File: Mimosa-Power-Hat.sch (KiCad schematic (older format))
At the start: 71 parts, among them J1 Screw_Terminal_01x04, J2 Screw_Terminal_01x02, J3 40HAT, J4 Screw_Terminal_01x02, J5 Screw_Terminal_01x04, J9 CONN_01X02, M1 Fan_Tacho_PWM, Q1 DMG2305UX, Q2 DMMT5401, U1 ADM3490ExR, U2 CAT24C32, U3 TCAN330, U5 AB0805, U6 MCP2515-xSO, U7 TXB0102DCU, U8 LM2678, Y1 32.768 kHz, Y2 8MHz

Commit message: Small update
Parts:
- added C?: 100nF, Capacitor_SMD:C_0805_2012Metric_Pad1.15x1.40mm_HandSolder, symbol Device:C
- added C?: C, Capacitor_SMD:C_0805_2012Metric_Pad1.15x1.40mm_HandSolder, symbol Device:C
- added D? (x4): LED, symbol Device:LED
- added J?: Screw_Terminal_01x02, TerminalBlock_Phoenix:TerminalBlock_Phoenix_MKDS-3-2-5.08_1x02_P5.08mm_Horizontal, symbol Connector:Screw_Terminal_01x02
- added R?: 250R, Resistor_SMD:R_0805_2012Metric_Pad1.15x1.40mm_HandSolder, symbol Device:R_Small
- added R? (x5): 1.2k, Resistor_SMD:R_0805_2012Metric_Pad1.15x1.40mm_HandSolder, symbol Device:R_Small
- added U?: H11L1, symbol Isolator:H11L1
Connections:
- net +3V3: now also C?.2, R?.2, R?.2, U?.6
- net +5V: now also R?.2
- net GND: now also C?.1, D?.1 (K), D?.1 (K), D?.1 (K), D?.1 (K), U?.5
- net P5V: now also R?.2
- net CLK-OUT: now reaches J3.33 (BCM13)
- net CLK-OUT: now also U6.3 (CLKOUT/SOF)
- net SeaTalk1: now reaches J3.37 (BCM26)
- net SeaTalk1: now also R?.1, U?.4
- new net: C?.1, R?.1, U?.1
- new net: D?.2 (A), R?.1 (x4)
- new net ST-Data: C?.2, J?.1 (Pin_1), R?.2, R?.2
- new net ST-GND: J?.2 (Pin_2), U?.2
- no-connect marks 30 -> 27
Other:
- note added: "SeaTalk 1 Read data"

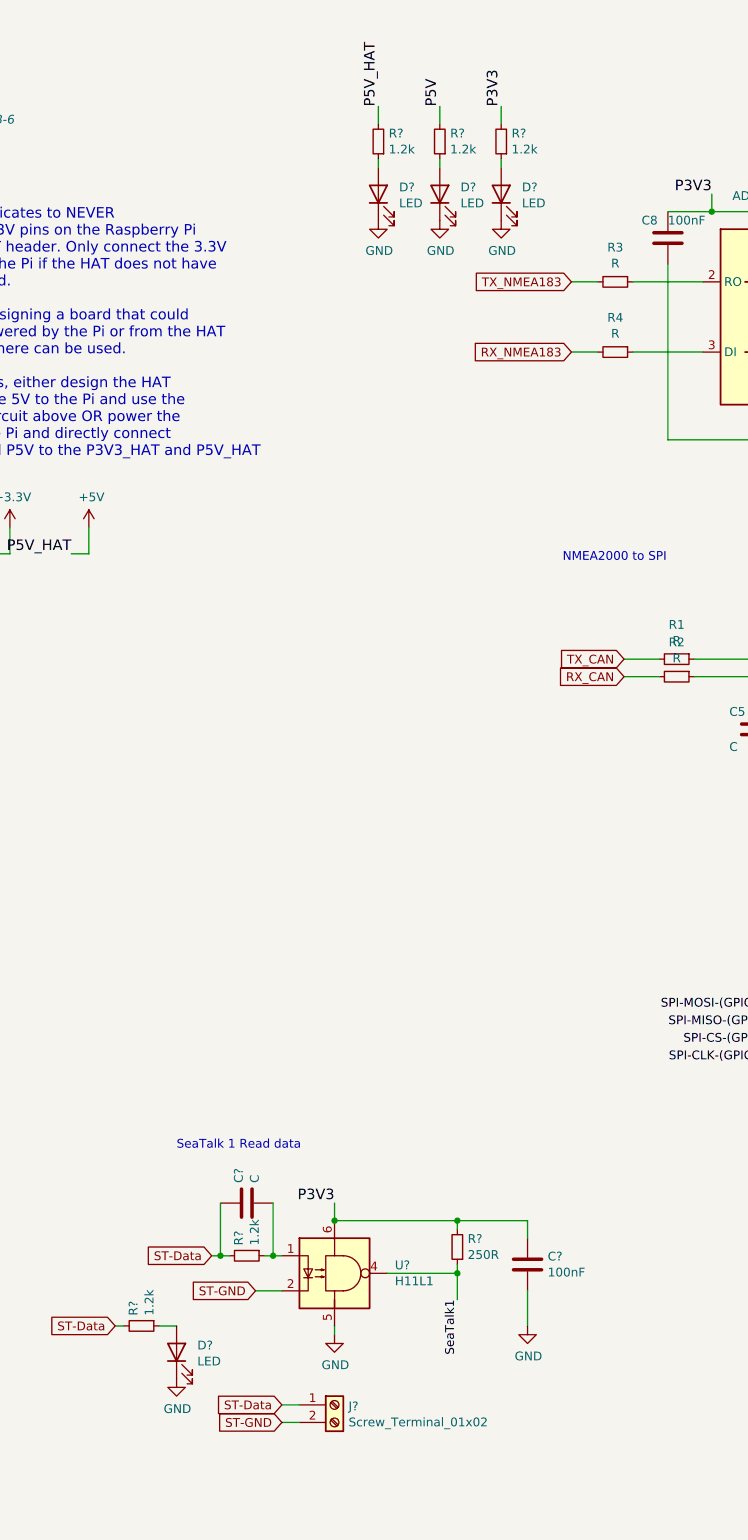
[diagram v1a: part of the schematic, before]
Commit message: Correction of NMEA2000 RX/TX inversion, addition of seatalk circuit connection (not yet routed)
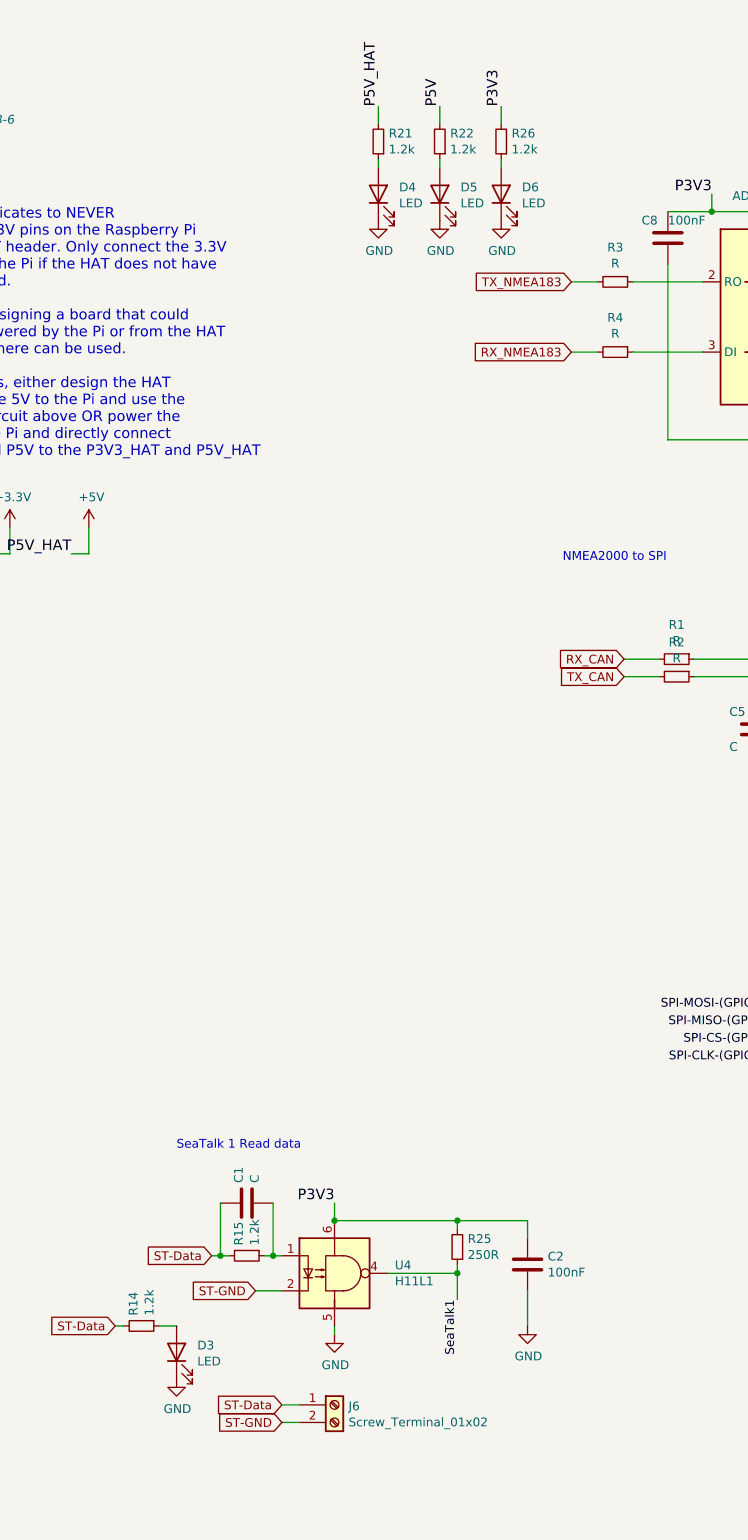
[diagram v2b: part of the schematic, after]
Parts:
- C1, C2: renamed from C?; footprint Capacitor_SMD:C_0805_2012Metric_Pad1.15x1.40mm_HandSolder -> Capacitor_SMD:C_0805_2012Metric_Pad1.18x1.45mm_HandSolder
- C11, C12, C13, C19, C20, C21, C22, C23, C24, C25, C26, C27, C5, C7, C8: footprint Capacitor_SMD:C_0805_2012Metric_Pad1.15x1.40mm_HandSolder -> Capacitor_SMD:C_0805_2012Metric_Pad1.18x1.45mm_HandSolder
- C32, C33: footprint Capacitor_SMD:C_0805_2012Metric -> Capacitor_SMD:C_0805_2012Metric_Pad1.18x1.45mm_HandSolder
- D3, D4, D5, D6: renamed from D?; footprint (none) -> LED_SMD:LED_0805_2012Metric
- R1, R10, R11, R12, R13, R16, R17, R18, R19, R2, R20, R23, R24, R29, R3, R4, R5, R6, R7, R8, R9: footprint Resistor_SMD:R_0805_2012Metric_Pad1.15x1.40mm_HandSolder -> Resistor_SMD:R_0805_2012Metric_Pad1.20x1.40mm_HandSolder
- R14, R15, R21, R22, R25, R26: renamed from R?; footprint Resistor_SMD:R_0805_2012Metric_Pad1.15x1.40mm_HandSolder -> Resistor_SMD:R_0805_2012Metric_Pad1.20x1.40mm_HandSolder
- U4: renamed from U?; footprint (none) -> Package_DIP:DIP-6_W7.62mm_LongPads
- gave numbers to parts that had none: 1
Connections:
- net RX_CAN: now also R1.2; no longer R2.2
- net TX_CAN: now also R2.2; no longer R1.2

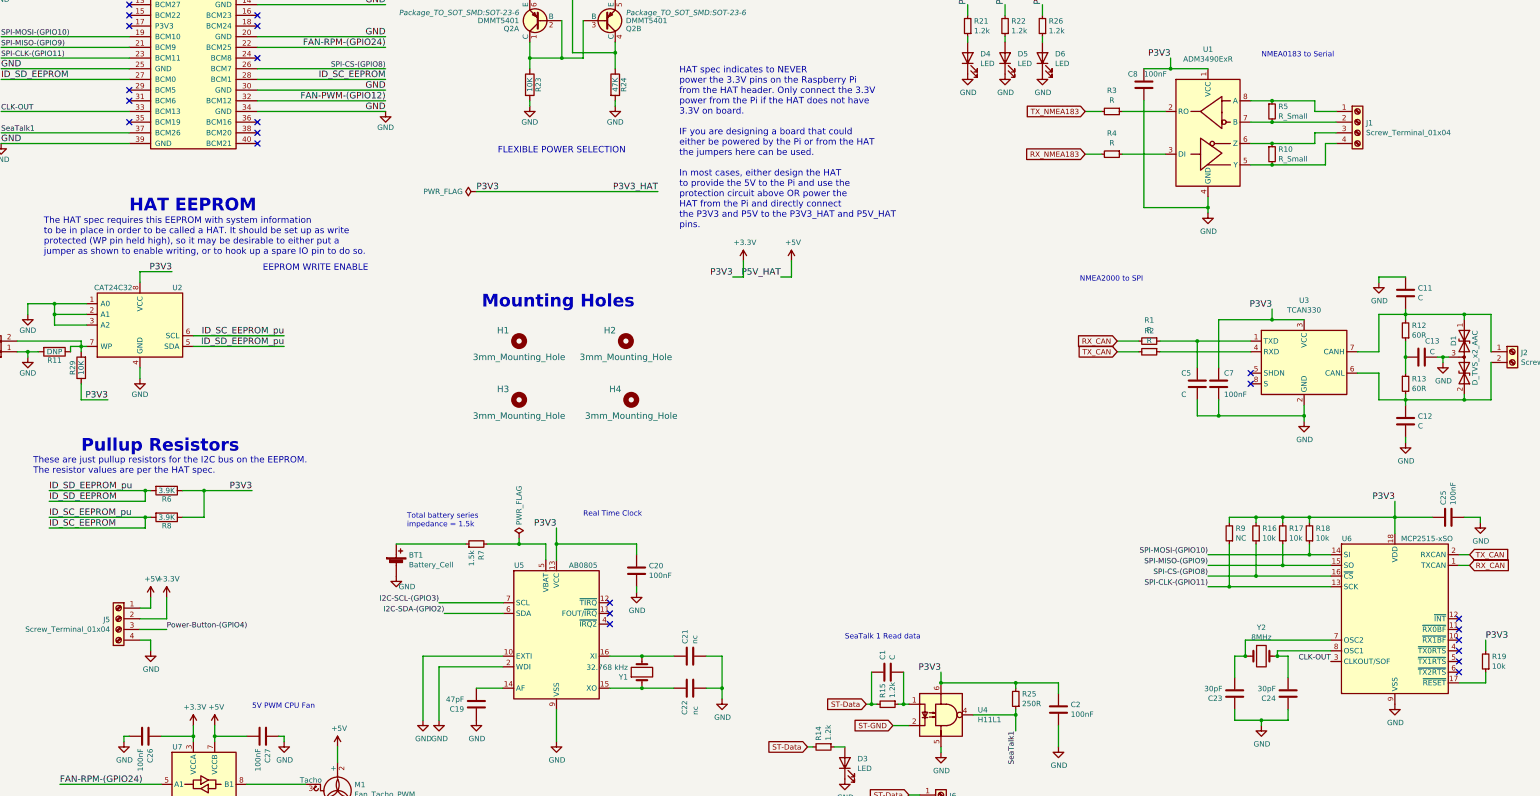
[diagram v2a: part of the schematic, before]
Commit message: add connection for seatalk, cleaned board and schematic
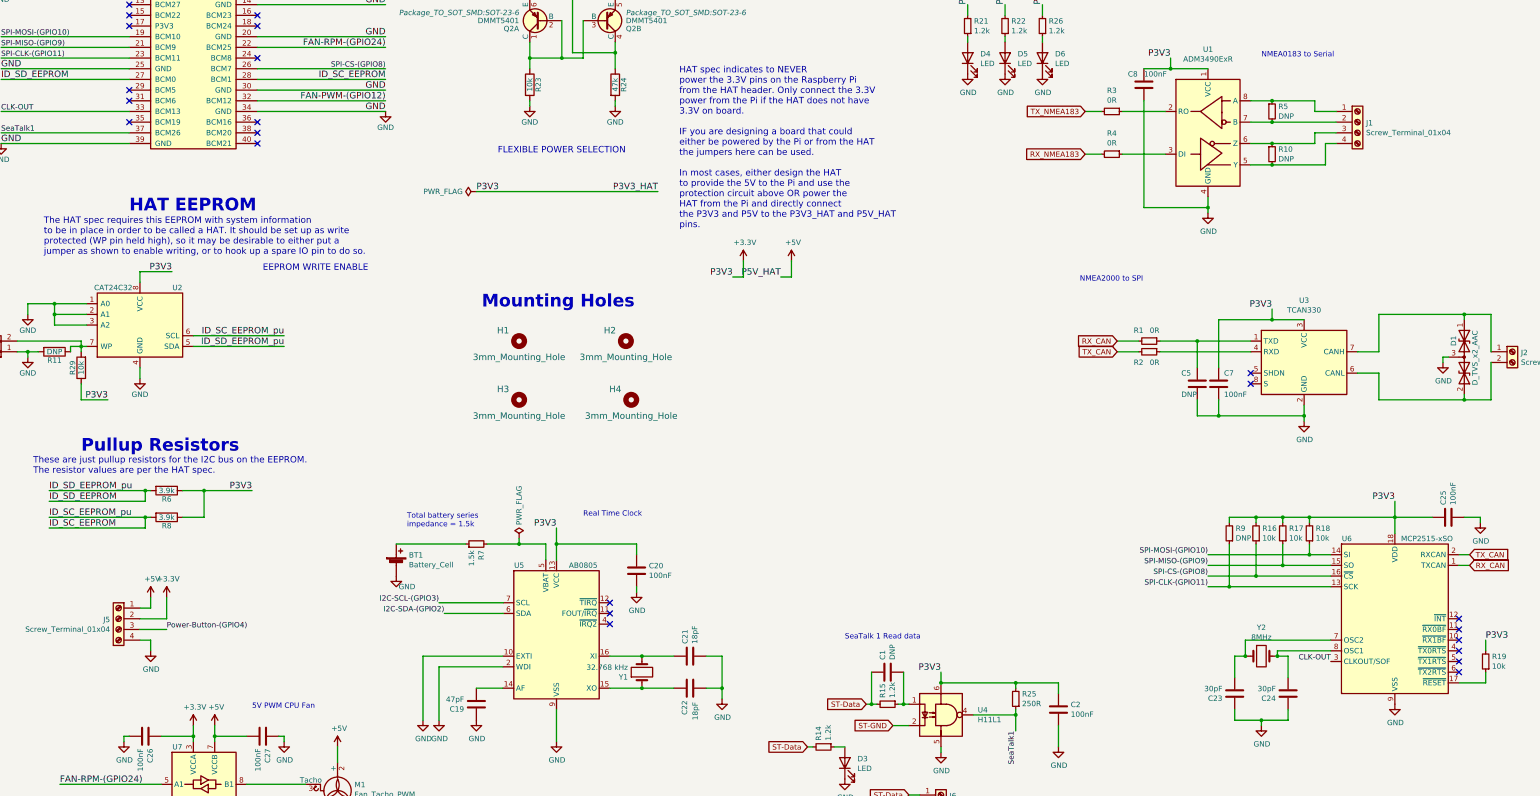
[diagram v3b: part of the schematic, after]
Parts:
- removed C11, C12, C13: C, Capacitor_SMD:C_0805_2012Metric_Pad1.18x1.45mm_HandSolder, symbol Device:C
- removed R12, R13: 60R, Resistor_SMD:R_0805_2012Metric_Pad1.20x1.40mm_HandSolder, symbol Device:R_Small
- C1, C5: value C -> DNP
- C21, C22: value nc -> 18pF
- R1, R2, R3, R4: value R -> 0R
- R10, R5: value R_Small -> DNP
- R23, R29: value 10K -> 10k
- R24: value 47K -> 47k
- R6, R8: value 3.9K -> 3.9k
- R9: value NC -> DNP
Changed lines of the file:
@@
 P 5750 3600
 F 0 "R23" V 5830 3600 50  0000 C CNN
-F 1 "10K" V 5750 3600 50  0000 C CNN
+F 1 "10k" V 5750 3600 50  0000 C CNN
 F 2 "Resistor_SMD:R_0805_2012Metric_Pad1.20x1.40mm_HandSolder" V 5680 3600 50  0001 C CNN
 F 3 "" H 5750 3600 50  0001 C CNN
@@
 P 6550 3600
 F 0 "R24" V 6630 3600 50  0000 C CNN
-F 1 "47K" V 6550 3600 50  0000 C CNN
+F 1 "47k" V 6550 3600 50  0000 C CNN
 F 2 "Resistor_SMD:R_0805_2012Metric_Pad1.20x1.40mm_HandSolder" V 6480 3600 50  0001 C CNN
 F 3 "" H 6550 3600 50  0001 C CNN
@@
 P 2350 7400
 F 0 "R6" V 2430 7400 50  0000 C CNN
-F 1 "3.9K" V 2350 7400 50  0000 C CNN
+F 1 "3.9k" V 2350 7400 50  0000 C CNN
 F 2 "Resistor_SMD:R_0805_2012Metric_Pad1.20x1.40mm_HandSolder" V 2280 7400 50  0001 C CNN
 F 3 "" H 2350 7400 50  0001 C CNN
@@
 P 2350 7650
 F 0 "R8" V 2430 7650 50  0000 C CNN
-F 1 "3.9K" V 2350 7650 50  0000 C CNN
+F 1 "3.9k" V 2350 7650 50  0000 C CNN
 F 2 "Resistor_SMD:R_0805_2012Metric_Pad1.20x1.40mm_HandSolder" V 2280 7650 50  0001 C CNN
 F 3 "" H 2350 7650 50  0001 C CNN
@@
 P 1550 6250
 F 0 "R29" V 1630 6250 50  0000 C CNN
-F 1 "10K" V 1550 6250 50  0000 C CNN
+F 1 "10k" V 1550 6250 50  0000 C CNN
 F 2 "Resistor_SMD:R_0805_2012Metric_Pad1.20x1.40mm_HandSolder" V 1480 6250 50  0001 C CNN
 F 3 "" H 1550 6250 50  0001 C CNN
@@
 P 12700 3850
 F 0 "R5" H 12759 3896 50  0000 L CNN
-F 1 "R_Small" H 12759 3805 50  0000 L CNN
+F 1 "DNP" H 12759 3805 50  0000 L CNN
 F 2 "Resistor_SMD:R_0805_2012Metric_Pad1.20x1.40mm_HandSolder" H 12700 3850 50  0001 C CNN
 F 3 "~" H 12700 3850 50  0001 C CNN
@@
 P 12700 4250
 F 0 "R10" H 12759 4296 50  0000 L CNN
-F 1 "R_Small" H 12759 4205 50  0000 L CNN
+F 1 "DNP" H 12759 4205 50  0000 L CNN
 F 2 "Resistor_SMD:R_0805_2012Metric_Pad1.20x1.40mm_HandSolder" H 12700 4250 50  0001 C CNN
 F 3 "~" H 12700 4250 50  0001 C CNN
@@
 F 3 "~" H 14950 6100 50  0001 C CNN
 	1    14950 6100
-	1    0    0    -1
-$EndComp
-$Comp
-L Device:R_Small R12
-U 1 1 5ECDFC7F
-P 13950 5900
-F 0 "R12" H 13891 5854 50  0000 R CNN
-F 1 "60R" H 13891 5945 50  0000 R CNN
-F 2 "Resistor_SMD:R_0805_2012Metric_Pad1.20x1.40mm_HandSolder" H 13950 5900 50  0001 C CNN
-F 3 "~" H 13950 5900 50  0001 C CNN
-	1    13950 5900
-	-1   0    0    1
-$EndComp
-$Comp
-L Device:R_Small R13
-U 1 1 5ECE0FD2
-P 13950 6400
-F 0 "R13" H 14009 6446 50  0000 L CNN
-F 1 "60R" H 14009 6355 50  0000 L CNN
-F 2 "Resistor_SMD:R_0805_2012Metric_Pad1.20x1.40mm_HandSolder" H 13950 6400 50  0001 C CNN
-F 3 "~" H 13950 6400 50  0001 C CNN
-	1    13950 6400
 	1    0    0    -1
 $EndComp
@@
 	0    1    1    0
 $EndComp
-$Comp
-L Device:C C13
-U 1 1 5ECEC47E
-P 14100 6150
-F 0 "C13" V 13950 6250 50  0000 C CNN
-F 1 "C" V 14050 6250 50  0000 C CNN
-F 2 "Capacitor_SMD:C_0805_2012Metric_Pad1.18x1.45mm_HandSolder" H 14138 6000 50  0001 C CNN
-F 3 "~" H 14100 6150 50  0001 C CNN
-	1    14100 6150
-	0    1    1    0
-$EndComp
-$Comp
-L Device:C C12
-U 1 1 5ECECBBD
-P 13950 6750
-F 0 "C12" H 13835 6704 50  0000 R CNN
-F 1 "C" H 13835 6795 50  0000 R CNN
-F 2 "Capacitor_SMD:C_0805_2012Metric_Pad1.18x1.45mm_HandSolder" H 13988 6600 50  0001 C CNN
-F 3 "~" H 13950 6750 50  0001 C CNN
-	1    13950 6750
-	-1   0    0    1
-$EndComp
-$Comp
-L Device:C C11
-U 1 1 5ECEDCFB
-P 13950 5550
-F 0 "C11" H 13835 5504 50  0000 R CNN
-F 1 "C" H 13835 5595 50  0000 R CNN
-F 2 "Capacitor_SMD:C_0805_2012Metric_Pad1.18x1.45mm_HandSolder" H 13988 5400 50  0001 C CNN
-F 3 "~" H 13950 5550 50  0001 C CNN
-	1    13950 5550
-	-1   0    0    1
-$EndComp
 Wire Wire Line
 	13500 6100 13700 6100
 Wire Wire Line
 	13700 6100 13700 5750
-Wire Wire Line
-	13700 5750 13950 5750
 Wire Wire Line
 	14750 5750 14750 6100
@@
 	14500 5750 14750 5750
 Wire Wire Line
-	13950 5800 13950 5750
-Connection ~ 13950 5750
-Wire Wire Line
-	13950 5750 14500 5750
-Wire Wire Line
-	13950 5750 13950 5700
-Wire Wire Line
 	13500 6300 13700 6300
 Wire Wire Line
 	13700 6300 13700 6550
-Wire Wire Line
-	13700 6550 13950 6550
 Wire Wire Line
 	14750 6550 14750 6200
@@
 	14500 6550 14750 6550
 Wire Wire Line
-	13950 6600 13950 6550
-Connection ~ 13950 6550
-Wire Wire Line
-	13950 6550 14500 6550
-Wire Wire Line
-	13950 6500 13950 6550
-Wire Wire Line
-	13950 6300 13950 6150
-Wire Wire Line
-	13950 6000 13950 6150
-Connection ~ 13950 6150
-Wire Wire Line
-	14250 6150 14300 6150
-Wire Wire Line
 	14300 6150 14300 6200
-Connection ~ 14300 6150
 Wire Wire Line
 	14300 6150 14350 6150
@@
 	1    0    0    -1
 $EndComp
-$Comp
-L power:GND #PWR011
-U 1 1 5ED52F52
-P 13950 6950
-F 0 "#PWR011" H 13950 6700 50  0001 C CNN
-F 1 "GND" H 13955 6777 50  0000 C CNN
-F 2 "" H 13950 6950 50  0001 C CNN
-F 3 "" H 13950 6950 50  0001 C CNN
-	1    13950 6950
-	1    0    0    -1
-$EndComp
-$Comp
-L power:GND #PWR010
-U 1 1 5ED533FE
-P 13700 5450
-F 0 "#PWR010" H 13700 5200 50  0001 C CNN
-F 1 "GND" H 13705 5277 50  0000 C CNN
-F 2 "" H 13700 5450 50  0001 C CNN
-F 3 "" H 13700 5450 50  0001 C CNN
-	1    13700 5450
-	1    0    0    -1
-$EndComp
-Wire Wire Line
-	13950 6900 13950 6950
-Wire Wire Line
-	13950 5400 13700 5400
-Wire Wire Line
-	13700 5400 13700 5450
 $Comp
 L Device:C C7
@@
 U 1 1 5EDB6ECB
 P 11550 6000
-F 0 "R1" V 11354 6000 50  0000 C CNN
-F 1 "R" V 11445 6000 50  0000 C CNN
+F 0 "R1" V 11450 5900 50  0000 C CNN
+F 1 "0R" V 11450 6050 50  0000 C CNN
 F 2 "Resistor_SMD:R_0805_2012Metric_Pad1.20x1.40mm_HandSolder" H 11550 6000 50  0001 C CNN
 F 3 "~" H 11550 6000 50  0001 C CNN
@@
 U 1 1 5EDB7435
 P 11550 6100
-F 0 "R2" V 11354 6100 50  0000 C CNN
-F 1 "R" V 11445 6100 50  0000 C CNN
+F 0 "R2" V 11650 6000 50  0000 C CNN
+F 1 "0R" V 11650 6150 50  0000 C CNN
 F 2 "Resistor_SMD:R_0805_2012Metric_Pad1.20x1.40mm_HandSolder" H 11550 6100 50  0001 C CNN
 F 3 "~" H 11550 6100 50  0001 C CNN
@@
 P 12000 6400
 F 0 "C5" H 12150 6300 50  0000 R CNN
-F 1 "C" H 12150 6500 50  0000 R CNN
+F 1 "DNP" H 12150 6500 50  0000 R CNN
 F 2 "Capacitor_SMD:C_0805_2012Metric_Pad1.18x1.45mm_HandSolder" H 12038 6250 50  0001 C CNN
 F 3 "~" H 12000 6400 50  0001 C CNN
@@
 P 11200 4250
 F 0 "R4" V 11004 4250 50  0000 C CNN
-F 1 "R" V 11095 4250 50  0000 C CNN
+F 1 "0R" V 11095 4250 50  0000 C CNN
 F 2 "Resistor_SMD:R_0805_2012Metric_Pad1.20x1.40mm_HandSolder" H 11200 4250 50  0001 C CNN
 F 3 "~" H 11200 4250 50  0001 C CNN
@@
 P 11200 3850
 F 0 "R3" V 11004 3850 50  0000 C CNN
-F 1 "R" V 11095 3850 50  0000 C CNN
+F 1 "0R" V 11095 3850 50  0000 C CNN
 F 2 "Resistor_SMD:R_0805_2012Metric_Pad1.20x1.40mm_HandSolder" H 11200 3850 50  0001 C CNN
 F 3 "~" H 11200 3850 50  0001 C CNN
@@
 P 12300 7800
 F 0 "R9" H 12241 7754 50  0000 R CNN
-F 1 "NC" H 12241 7845 50  0000 R CNN
+F 1 "DNP" H 12241 7845 50  0000 R CNN
 F 2 "Resistor_SMD:R_0805_2012Metric_Pad1.20x1.40mm_HandSolder" H 12300 7800 50  0001 C CNN
 F 3 "~" H 12300 7800 50  0001 C CNN
@@
 P 7250 8950
 F 0 "C21" H 7135 8904 50  0000 R CNN
-F 1 "nc" H 7135 8995 50  0000 R CNN
+F 1 "18pF" H 7135 8995 50  0000 R CNN
 F 2 "Capacitor_SMD:C_0805_2012Metric_Pad1.18x1.45mm_HandSolder" H 7288 8800 50  0001 C CNN
 F 3 "~" H 7250 8950 50  0001 C CNN
@@
 P 7250 9250
 F 0 "C22" H 7500 9200 50  0000 R CNN
-F 1 "nc" H 7500 9300 50  0000 R CNN
+F 1 "18pF" H 7550 9300 50  0000 R CNN
 F 2 "Capacitor_SMD:C_0805_2012Metric_Pad1.18x1.45mm_HandSolder" H 7288 9100 50  0001 C CNN
 F 3 "~" H 7250 9250 50  0001 C CNN
@@
 P 9100 9100
 F 0 "C1" H 8985 9054 50  0000 R CNN
-F 1 "C" H 8985 9145 50  0000 R CNN
+F 1 "DNP" H 8985 9145 50  0000 R CNN
 F 2 "Capacitor_SMD:C_0805_2012Metric_Pad1.18x1.45mm_HandSolder" H 9138 8950 50  0001 C CNN
 F 3 "~" H 9100 9100 50  0001 C CNN
@@
 	1    0    0    -1
 $EndComp
+Wire Wire Line
+	13700 5750 14500 5750
+Wire Wire Line
+	13700 6550 14500 6550
 $EndSCHEMATC
